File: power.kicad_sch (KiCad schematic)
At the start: 33 parts, among them U5 TPS82084SIL, U6 TPS82084SIL, U7 TPS7A8801RTJR

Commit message: Minor tidy ups and fix a stupid bug.
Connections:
- net FbCG18 renamed Fb1V8
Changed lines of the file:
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@@
-	(wire
-		(pts
-			(xy 203.2 31.75) (xy 215.9 31.75)
-		)
-		(stroke
-			(width 0)
-			(type default)
-		)
-	)
 	(wire
 		(pts
@@
 		)
 	)
-	(label "FbCG18"
+	(label "Fb1V8"
 		(at 182.88 39.37 0)
 		(effects
@@
 		(length 2.54)
 		(shape round)
-		(at 208.28 31.75 0)
+		(at 186.69 31.75 0)
 		(fields_autoplaced yes)
 		(effects
@@
 		)
 		(property "Netclass" "Pwr"
-			(at 208.9785 29.21 0)
+			(at 187.3885 29.21 0)
 			(effects
 				(font
@@
 		)
 		(property "Component Class" ""
-			(at 147.32 -45.72 0)
+			(at 125.73 -45.72 0)
 			(effects
 				(font
@@
 		(length 2.54)
 		(shape round)
-		(at 147.32 66.04 0)
+		(at 140.97 66.04 0)
 		(fields_autoplaced yes)
 		(effects
@@
 		)
 		(property "Netclass" "Pwr"
-			(at 148.0185 63.5 0)
+			(at 141.6685 63.5 0)
 			(effects
 				(font
@@
 		)
 		(property "Component Class" ""
-			(at 86.36 -11.43 0)
+			(at 80.01 -11.43 0)
 			(effects
 				(font
@@
 	(symbol
 		(lib_id "power:+1V8")
-		(at 215.9 31.75 0)
+		(at 203.2 31.75 0)
 		(unit 1)
 		(exclude_from_sim no)
@@
 		(dnp no)
 		(property "Reference" "#PWR059"
-			(at 215.9 35.56 0)
+			(at 203.2 35.56 0)
 			(effects
 				(font
@@
 		)
 		(property "Value" "+1V8"
-			(at 215.9 28.194 0)
+			(at 203.2 28.194 0)
 			(effects
 				(font
@@
 		)
 		(property "Footprint" ""
-			(at 215.9 31.75 0)
+			(at 203.2 31.75 0)
 			(effects
 				(font
@@
 		)
 		(property "Datasheet" ""
-			(at 215.9 31.75 0)
+			(at 203.2 31.75 0)
 			(effects
 				(font
@@
 		)
 		(property "Description" "Power symbol creates a global label with name \"+1V8\""
-			(at 215.9 31.75 0)
-			(effects
-				(font
+			(at 203.2 31.75 0)
+			(effects
+				(font

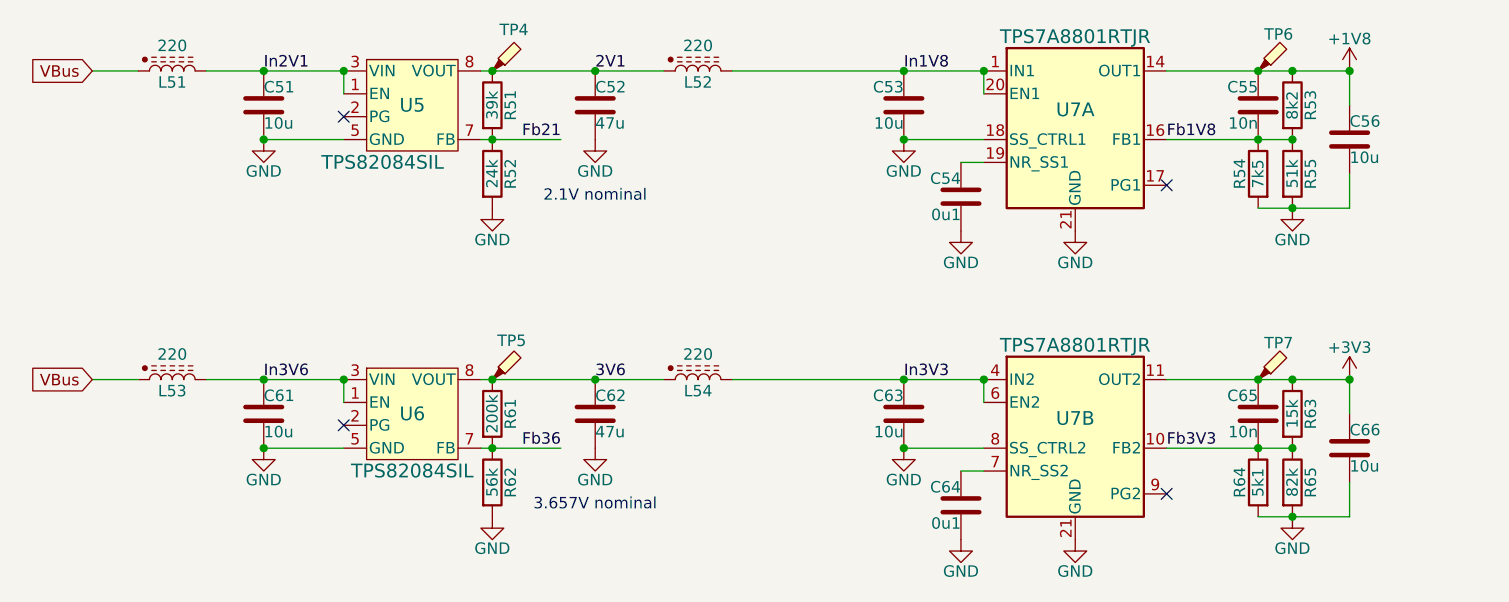
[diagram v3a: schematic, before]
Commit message: FPGA in, layout mostly updated.
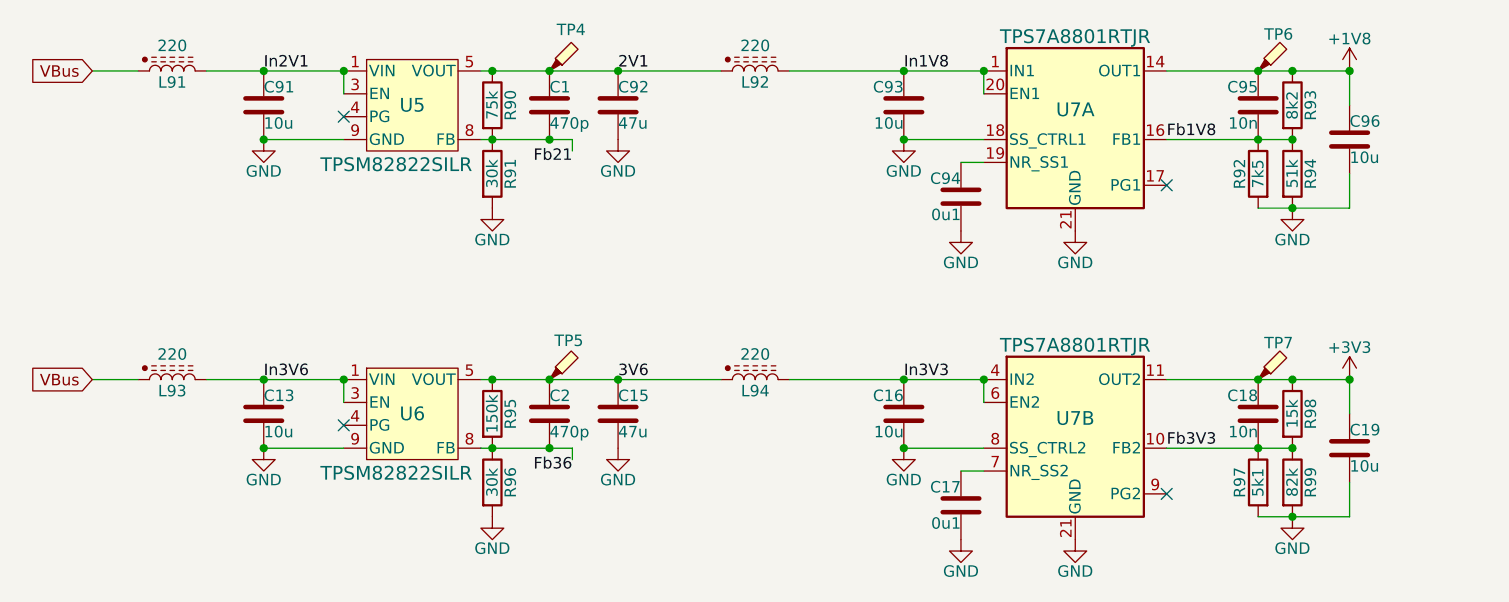
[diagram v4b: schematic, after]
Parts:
- added C1, C2: 470p, Capacitor_SMD:C_0402_1005Metric, symbol Device:C
- C13: renamed from C61; footprint Capacitor_SMD:C_0402_1005Metric -> Capacitor_SMD:C_0603_1608Metric; LCSC C15525 -> C96446
- C16: renamed from C63; footprint Capacitor_SMD:C_0402_1005Metric -> Capacitor_SMD:C_0603_1608Metric
- C91: renamed from C51; footprint Capacitor_SMD:C_0402_1005Metric -> Capacitor_SMD:C_0603_1608Metric; LCSC C15525 -> C96446
- C93: renamed from C53; footprint Capacitor_SMD:C_0402_1005Metric -> Capacitor_SMD:C_0603_1608Metric
- R90: renamed from R51; value 39k -> 75k; LCSC C25783 -> C25798
- R91: renamed from R52; value 24k -> 30k; footprint Resistor_SMD:R_0402_1005Metric -> Resistor_SMD:R_0603_1608Metric; LCSC C25769 -> C22984
- R95: renamed from R61; value 200k -> 150k; LCSC C25764 -> C25755
- R96: renamed from R62; value 56k -> 30k; footprint Resistor_SMD:R_0402_1005Metric -> Resistor_SMD:R_0603_1608Metric; LCSC C25796 -> C22984
- TP4: value TestPoint_Probe -> 2V2
- U5, U6: value TPS82084SIL -> TPSM82822SILR; footprint Parts:SIL0008C_SMD_NV -> Parts:SIL0010D-MFG; symbol Parts:TPS82084SIL -> Parts:TPSM82822SILR
- renumbered C62 to C15, C64 to C17, C65 to C18, C66 to C19, C52 to C92, C54 to C94, C55 to C95, C56 to C96, L51 to L91, L52 to L92, L53 to L93, L54 to L94, R54 to R92, R53 to R93, R55 to R94, R64 to R97, R63 to R98, R65 to R99
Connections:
- net 2V1: now also U5.5 (VOUT), U5.6 (VOUT), U5.7 (VOUT), C1.1; no longer U5.8 (VOUT)
- net 3V6: now also U6.5 (VOUT), U6.6 (VOUT), U6.7 (VOUT), C2.1; no longer U6.8 (VOUT)
- net Fb21: now also U5.8 (FB), C1.2; no longer U5.7 (FB)
- net Fb36: now also U6.8 (FB), C2.2; no longer U6.7 (FB)
- net GND: now also U5.10 (GND), U6.10 (GND); no longer U5.5 (GND), U5.6 (GND), U6.5 (GND), U6.6 (GND)
- net In2V1: now also U5.2 (VIN); no longer U5.4 (VIN)
- net In3V6: now also U6.2 (VIN); no longer U6.4 (VIN)
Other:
- note removed: "2.1V nominal"
- note removed: "3.657V nominal"
- moved on the sheet: C15, C92, L92, L94, TP4, TP5

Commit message: Layout down
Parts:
- added C19, C97: 22u, Capacitor_SMD:C_0603_1608Metric, symbol Device:C
- C1, C2, R90, R92, R93, R95: Stock (none) -> Prom
- C13, C15, C91, C92, C94, C95, C96, R91, R96, R97, R98, R99: Stock (none) -> Basic
- C16, C93: LCSC C15525 -> C96446; Stock (none) -> Basic
- C17: renamed from C18; Stock (none) -> Basic
- C18: renamed from C19; Stock (none) -> Basic
- C20: renamed from C17; Stock (none) -> Basic
- L91, L92, L93, L94: value 220 -> 120; Stock (none) -> Basic
- R94: footprint Resistor_SMD:R_0603_1608Metric -> Resistor_SMD:R_0402_1005Metric; LCSC C23196 -> C25794; Stock (none) -> Basic
- TP4, TP5, TP6, TP7: Stock (none) -> N/A
- U5, U6: LCSC C468248 -> C5219367; Stock (none) -> Ext
- U7: Stock (none) -> 4
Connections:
- net +1V8: now also C97.1
- net +3V3: now also C19.1
- net GND: now also C19.2, C97.2

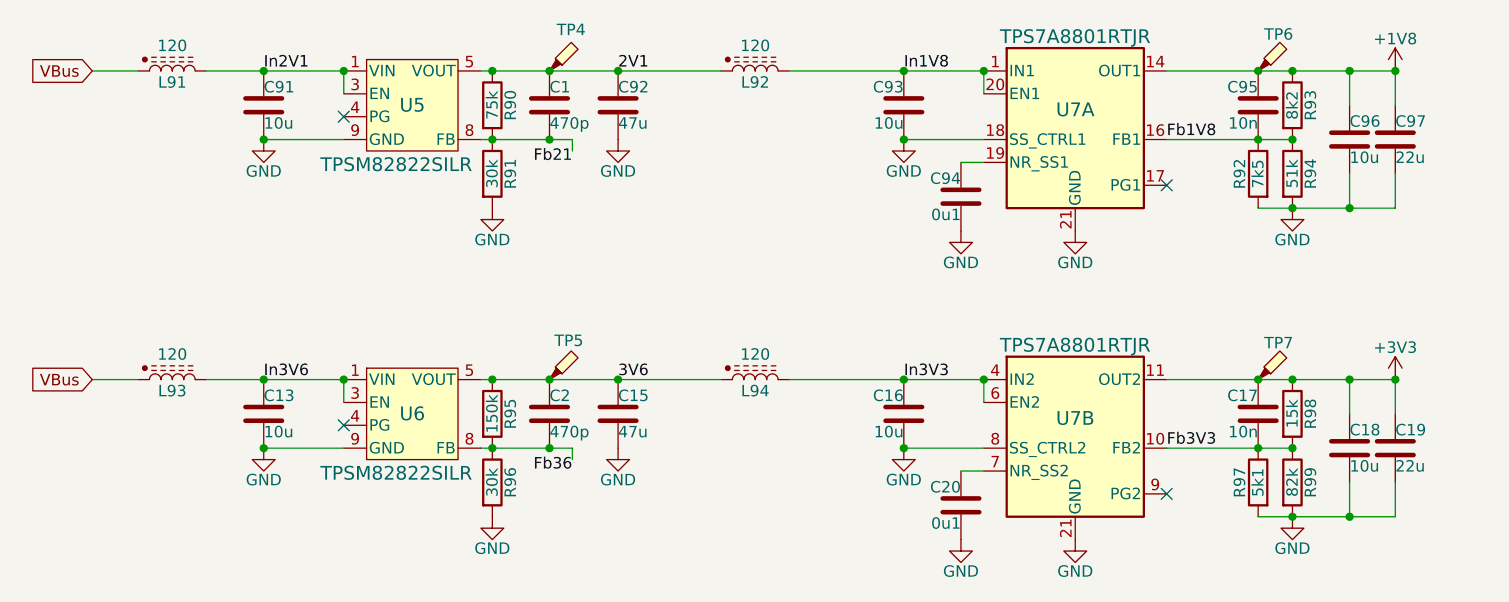
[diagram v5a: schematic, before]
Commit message: Pull-up on safe-boot.  Juggle things a bit.
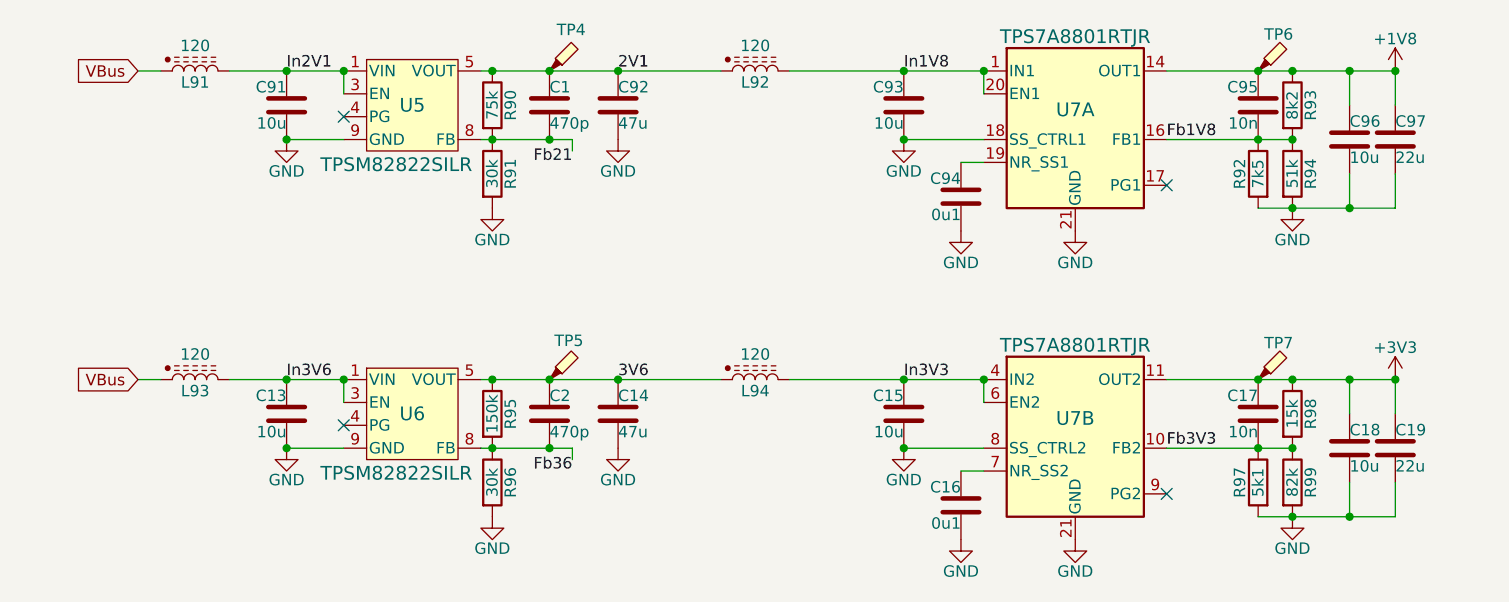
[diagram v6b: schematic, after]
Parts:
- renumbered C15 to C14, C16 to C15, C20 to C16
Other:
- moved on the sheet: C13, C91, L91, L93

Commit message: Back to tps82084...
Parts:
- removed C1, C2: 470p, Capacitor_SMD:C_0402_1005Metric, symbol Device:C
- R90: value 75k -> 39k; LCSC C25798 -> C25783; Stock Prom -> (none)
- R91: value 30k -> 24k; footprint Resistor_SMD:R_0603_1608Metric -> Resistor_SMD:R_0402_1005Metric; LCSC C22984 -> C25769; Stock Basic -> (none)
- R95: value 150k -> 200k; LCSC C25755 -> C25764
- R96: value 30k -> 46k; footprint Resistor_SMD:R_0603_1608Metric -> Resistor_SMD:R_0402_1005Metric; LCSC C22984 -> C25764
- U5, U6: value TPSM82822SILR -> TPS82084SIL; footprint Parts:SIL0010D-MFG -> Parts:SIL0008C_SMD_NV; symbol Parts:TPSM82822SILR -> Parts:TPS82084SIL; LCSC C5219367 -> C468248
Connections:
- net 2V1: now also U5.8 (VOUT); no longer U5.5 (VOUT), U5.6 (VOUT), U5.7 (VOUT)
- net 3V6: now also U6.8 (VOUT); no longer U6.5 (VOUT), U6.6 (VOUT), U6.7 (VOUT)
- net Fb21: now also U5.7 (FB); no longer U5.8 (FB)
- net Fb36: now also U6.7 (FB); no longer U6.8 (FB)
- net GND: now also U5.5 (GND), U5.6 (GND), U6.5 (GND), U6.6 (GND); no longer U5.10 (GND), U6.10 (GND)
- net In2V1: now also U5.4 (VIN); no longer U5.2 (VIN)
- net In3V6: now also U6.4 (VIN); no longer U6.2 (VIN)

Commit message: Ordered.
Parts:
- R90, R91: Stock (none) -> Prom
- R96: value 46k -> 56k; LCSC C25764 -> C25796
- U7: now left out of the parts list
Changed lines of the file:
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@@
 		(body_style 1)
 		(exclude_from_sim no)
-		(in_bom yes)
+		(in_bom no)
 		(on_board yes)
 		(in_pos_files yes)
@@
 			)
 		)
-		(property "Stock" ""
+		(property "Stock" "Prom"
 			(at 107.95 35.56 90)
 			(hide yes)
@@
 			)
 		)
-		(property "Stock" ""
+		(property "Stock" "Prom"
 			(at 107.95 43.18 90)
 			(hide yes)
@@
 		(body_style 1)
 		(exclude_from_sim no)
-		(in_bom yes)
+		(in_bom no)
 		(on_board yes)
 		(in_pos_files yes)
@@
 			)
 		)
-		(property "Value" "46k"
+		(property "Value" "56k"
 			(at 107.95 77.47 90)
 			(show_name no)
@@
 			)
 		)
-		(property "LCSC" "C25764"
+		(property "LCSC" "C25796"
 			(at 107.95 77.47 90)
 			(hide yes)
